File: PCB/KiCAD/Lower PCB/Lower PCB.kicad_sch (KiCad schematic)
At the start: 94 parts, among them IC1 ADG608BRZ, IC2 ADG608BRZ, J1 Conn_01x04, J2 Conn_01x02, J3 Conn_01x08, Q1 SFH320, Q10 SFH320, Q11 SFH320, Q12 SFH320, Q13 SFH320, Q14 SFH320, Q15 SFH320, Q16 SFH320, Q2 SFH320, Q3 SFH320, Q4 SFH320, Q5 SFH320, Q6 SFH320, Q7 SFH320, Q8 SFH320, Q9 SFH320, U1 ATmega328PB-A, Y1 Crystal

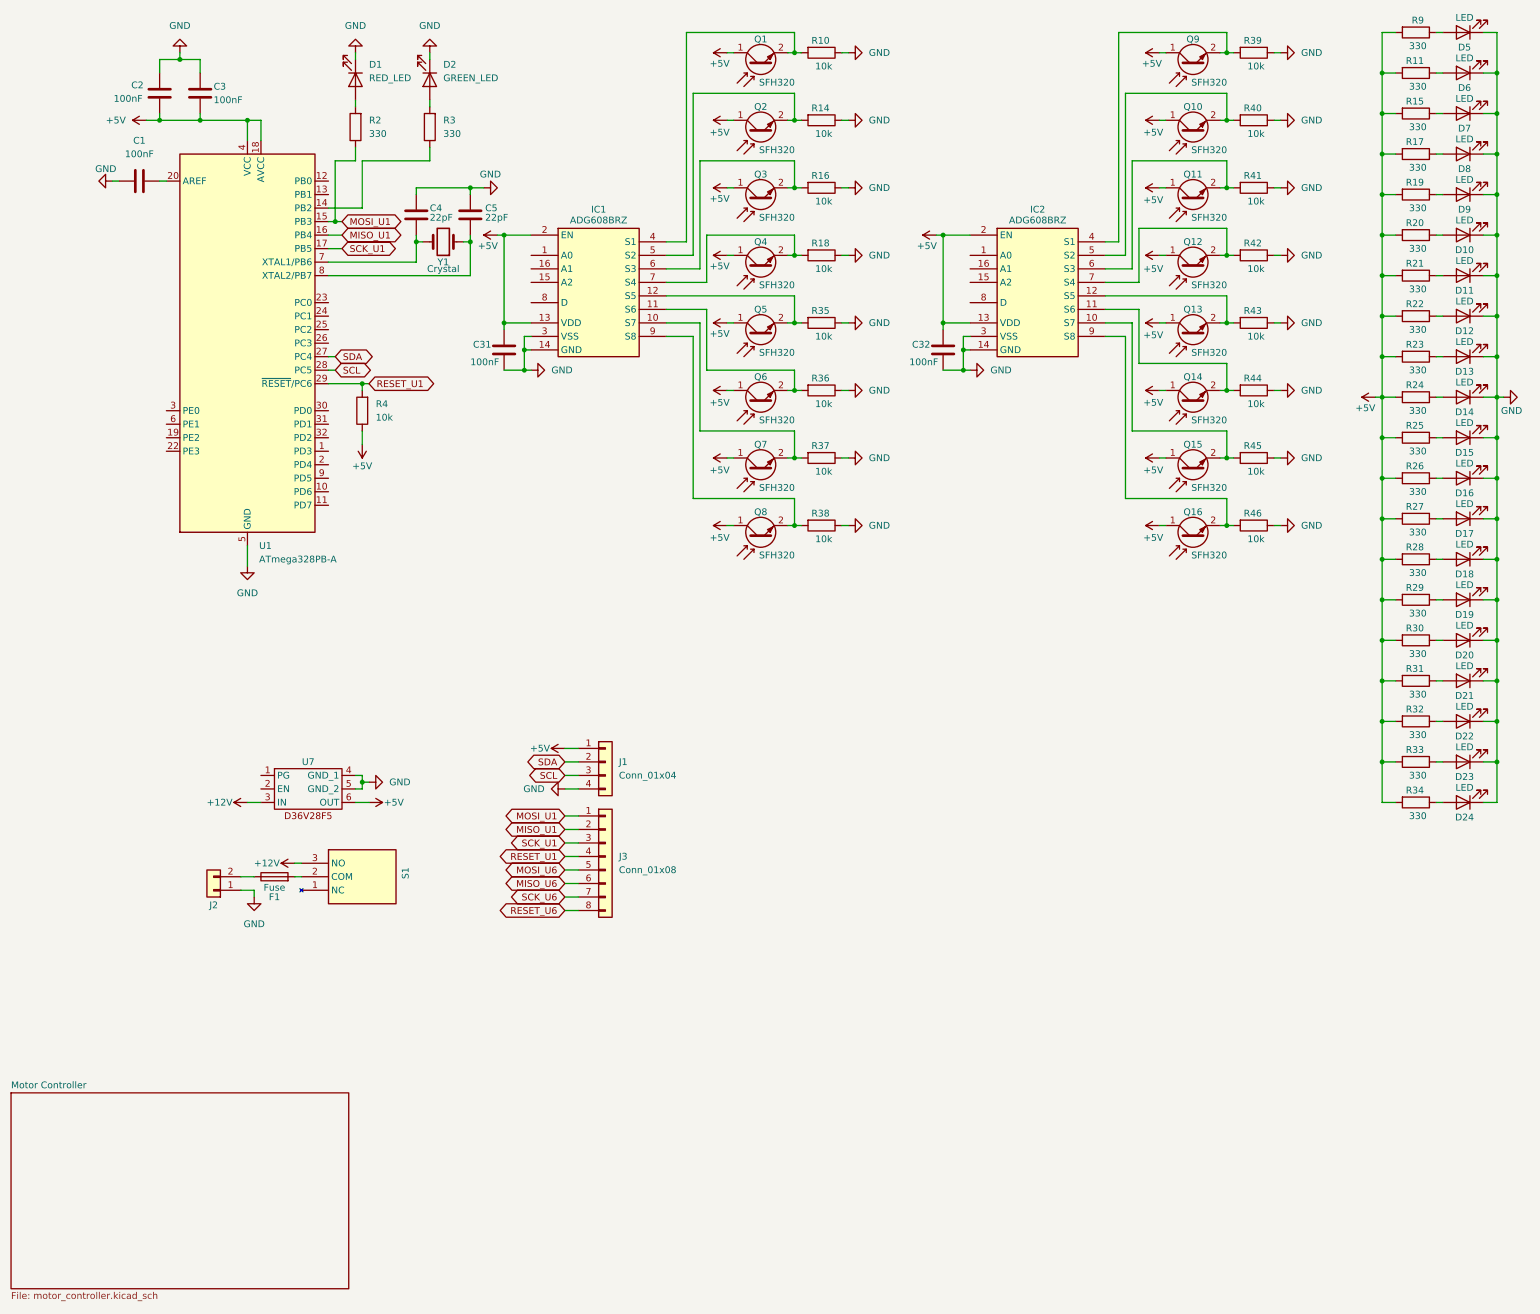
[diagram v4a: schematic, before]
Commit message: Redone main PCB traces and started lower PCB
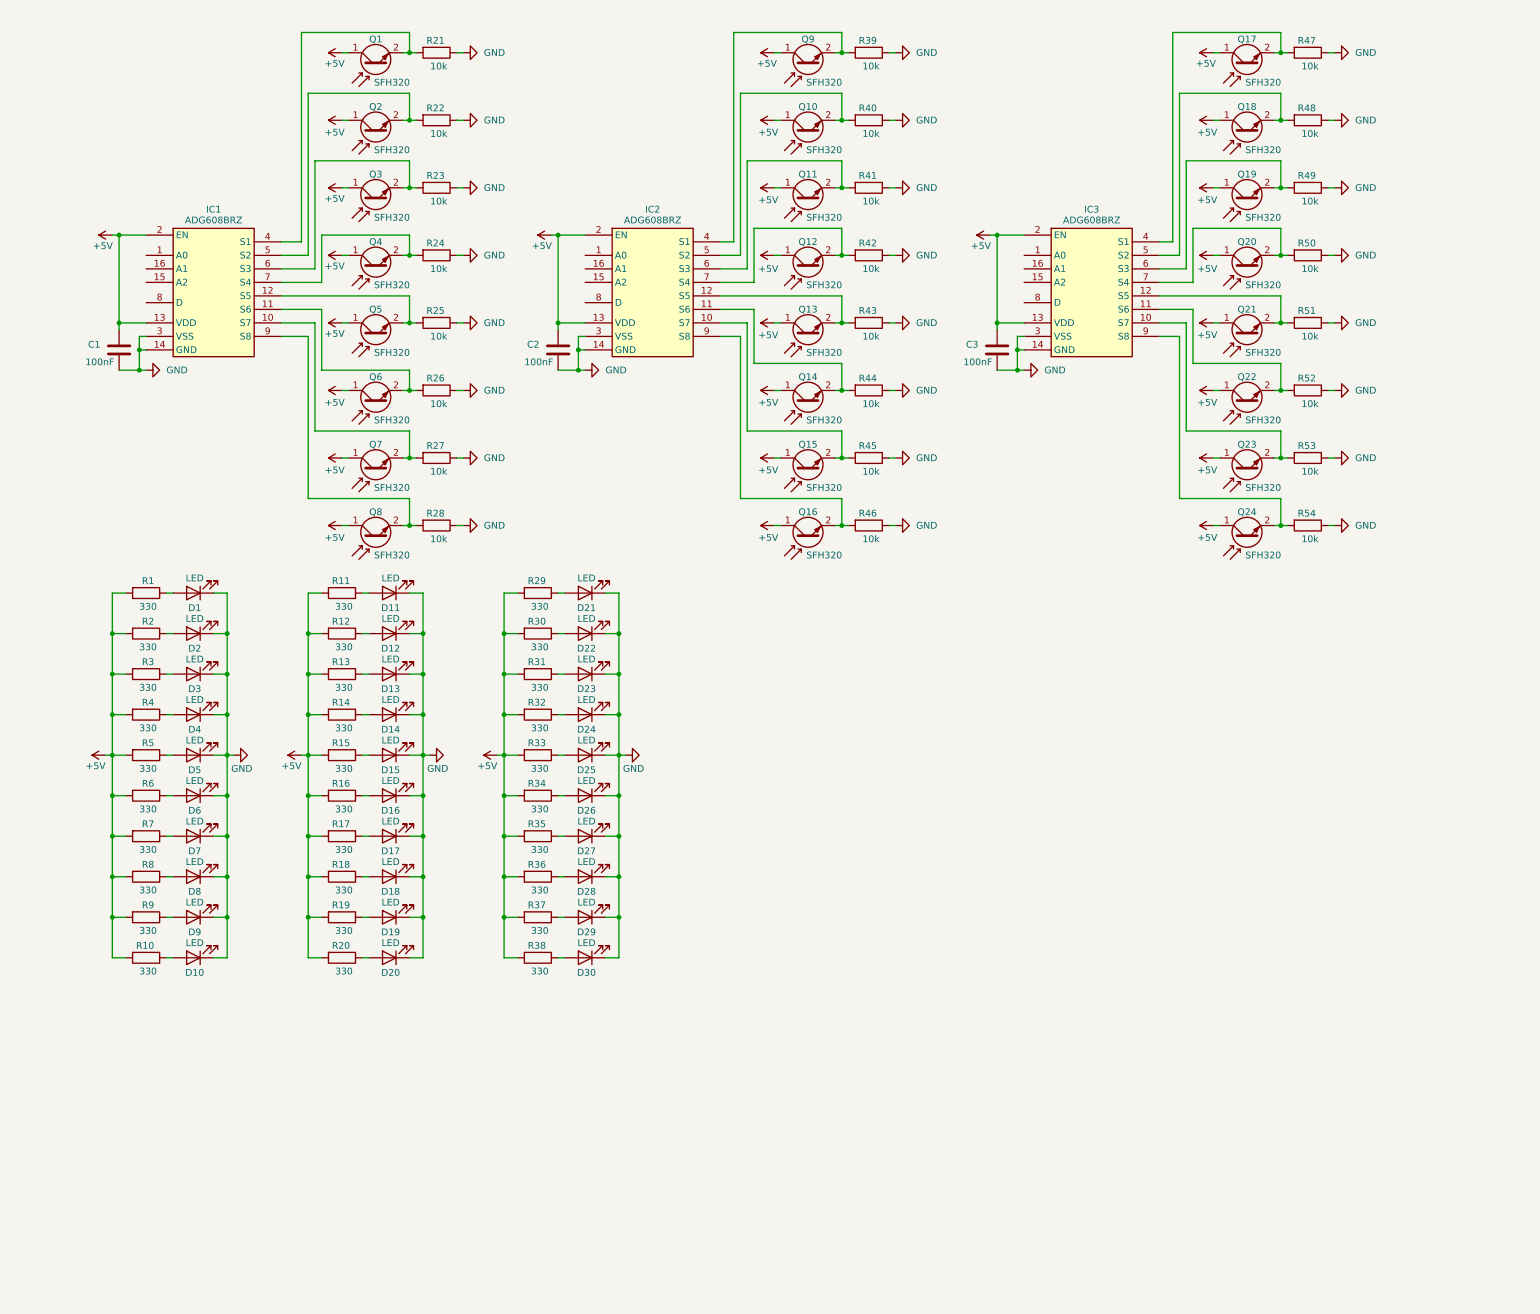
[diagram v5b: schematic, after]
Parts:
- removed C1, C2: 100nF, Capacitor_SMD:C_0805_2012Metric_Pad1.18x1.45mm_HandSolder, symbol Device:C
- removed C4, C5: 22pF, Capacitor_SMD:C_0805_2012Metric_Pad1.18x1.45mm_HandSolder, symbol Device:C
- removed D1: RED_LED, LED_SMD:LED_0805_2012Metric_Pad1.15x1.40mm_HandSolder, symbol Device:LED
- removed D2: GREEN_LED, LED_SMD:LED_0805_2012Metric_Pad1.15x1.40mm_HandSolder, symbol Device:LED
- removed F1: Fuse, Fuse:Fuseholder_Blade_Mini_Keystone_3568, symbol Device:Fuse
- removed J1: Conn_01x04, Connector_JST:JST_PH_B4B-PH-K_1x04_P2.00mm_Vertical, symbol Connector_Generic:Conn_01x04
- removed J2: Conn_01x02, Connector_AMASS:AMASS_XT60-M_1x02_P7.20mm_Vertical, symbol Connector_Generic:Conn_01x02
- removed J3: Conn_01x08, Connector_JST:JST_PH_B8B-PH-K_1x08_P2.00mm_Vertical, symbol Connector_Generic:Conn_01x08
- removed R2, R3: 330, Resistor_SMD:R_0805_2012Metric_Pad1.20x1.40mm_HandSolder, symbol Device:R
- removed R4: 10k, Resistor_SMD:R_0805_2012Metric_Pad1.20x1.40mm_HandSolder, symbol Device:R
- removed S1: 1101M2S3CGE2, 1101M2S3CGE2:1101M2S3CGE2, symbol 1101M2S3CGE2:1101M2S3CGE2
- removed U1: ATmega328PB-A, Package_QFP:TQFP-32_7x7mm_P0.8mm, symbol MCU_Microchip_ATmega:ATmega328PB-A
- removed U7: ~, Pololu:D36V28F5, symbol Pololu:D36V28F5
- removed Y1: Crystal, Crystal:Crystal_SMD_HC49-SD, symbol Device:Crystal
- added D21, D22, D23, D24, D25, D26, D27, D28, D29, D30: LED, LED_SMD:LED_PLCC-2_3.4x3.0mm_KA, symbol Device:LED
- added IC3: ADG608BRZ, ADG608BRZ:SOIC127P600X175-16N, symbol ADG608BRZ:ADG608BRZ
- added Q17, Q18, Q19, Q20, Q21, Q22, Q23, Q24: SFH320, LED_SMD:LED_PLCC-2_3.4x3.0mm_KA, symbol Sensor_Optical:SFH320
- added R29, R30, R31, R32, R33, R34, R35, R36, R37, R38: 330, Resistor_SMD:R_0805_2012Metric_Pad1.20x1.40mm_HandSolder, symbol Device:R
- added R47, R48, R49, R50, R51, R52, R53, R54: 10k, Resistor_SMD:R_0805_2012Metric_Pad1.20x1.40mm_HandSolder, symbol Device:R
- renumbered C31 to C1, C32 to C2, D5 to D1, D14 to D10, D15 to D11, D16 to D12, D17 to D13, D18 to D14, D19 to D15, D20 to D16, D21 to D17, D22 to D18, D23 to D19, D6 to D2, D24 to D20, D7 to D3, D8 to D4, D9 to D5, D10 to D6, D11 to D7, D12 to D8, D13 to D9, R9 to R1, R24 to R10, R25 to R11, R26 to R12, R27 to R13, R28 to R14, R29 to R15, R30 to R16, R31 to R17, R32 to R18, R33 to R19, R11 to R2, R34 to R20, R10 to R21, R14 to R22, R16 to R23, R18 to R24, R35 to R25, R36 to R26, R37 to R27, R38 to R28, R15 to R3, R17 to R4, R19 to R5, R20 to R6, R21 to R7, R22 to R8, R23 to R9
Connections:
- net +5V: now also C3.1, IC3.13 (VDD), IC3.2 (EN), Q17.1 (C), Q18.1 (C), Q19.1 (C), Q20.1 (C), Q21.1 (C), Q22.1 (C), Q23.1 (C), Q24.1 (C), R29.2, R30.2, R31.2, R32.2, R33.2, R34.2, R35.2, R36.2, R37.2, R38.2; no longer C3.2
- net GND: now also C3.2, D21.1 (K), D22.1 (K), D23.1 (K), D24.1 (K), D25.1 (K), D26.1 (K), D27.1 (K), D28.1 (K), D29.1 (K), D30.1 (K), IC3.14 (GND), IC3.3 (VSS), R47.1, R48.1, R49.1, R50.1, R51.1, R52.1, R53.1, R54.1; no longer C3.1
- new net: IC3.9 (S8), Q24.2 (E), R54.2
- new net: IC3.12 (S5), Q21.2 (E), R51.2
- new net: D30.2 (A), R38.1
- new net: IC3.7 (S4), Q20.2 (E), R50.2
- new net: D27.2 (A), R35.1
- new net: IC3.4 (S1), Q17.2 (E), R47.2
- new net: D23.2 (A), R31.1
- new net: D24.2 (A), R32.1
- new net: IC3.11 (S6), Q22.2 (E), R52.2
- new net: IC3.10 (S7), Q23.2 (E), R53.2
- new net: D26.2 (A), R34.1
- new net: D21.2 (A), R29.1
- new net: D28.2 (A), R36.1
- new net: IC3.6 (S3), Q19.2 (E), R49.2
- new net: IC3.5 (S2), Q18.2 (E), R48.2
- new net: D29.2 (A), R37.1
- new net: D25.2 (A), R33.1
- new net: D22.2 (A), R30.1
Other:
- removed sheet Motor Controller
- moved on the sheet: C1, C2, D1, D10, D11, D12, D13, D14, D15, D16, D17, D18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

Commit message: Work on the lower PCB
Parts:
- added J1, J2, J3: Conn_01x04_MountingPin, Connector_JST:JST_PH_B4B-PH-SM4-TB_1x04-1MP_P2.00mm_Vertical, symbol Connector_Generic_MountingPin:Conn_01x04_MountingPin
- added J4: Conn_01x02_MountingPin, Connector_JST:JST_PH_B2B-PH-SM4-TB_1x02-1MP_P2.00mm_Vertical, symbol Connector_Generic_MountingPin:Conn_01x02_MountingPin
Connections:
- net GND: now also J4.2 (Pin_2)
- new net +3V3: J4.1 (Pin_1)
- new net LED_1_A0: J1.2 (Pin_2)
- new net LED_1_A1: J1.3 (Pin_3)
- new net LED_1_A2: J1.4 (Pin_4)
- new net LED_1_OUT: J1.1 (Pin_1)
- new net LED_2_A0: J2.2 (Pin_2)
- new net LED_2_A1: J2.3 (Pin_3)
- new net LED_2_A2: J2.4 (Pin_4)
- new net LED_2_OUT: J2.1 (Pin_1)
- new net LED_3_A0: J3.2 (Pin_2)
- new net LED_3_A1: J3.3 (Pin_3)
- new net LED_3_A2: J3.4 (Pin_4)
- new net LED_3_OUT: J3.1 (Pin_1)

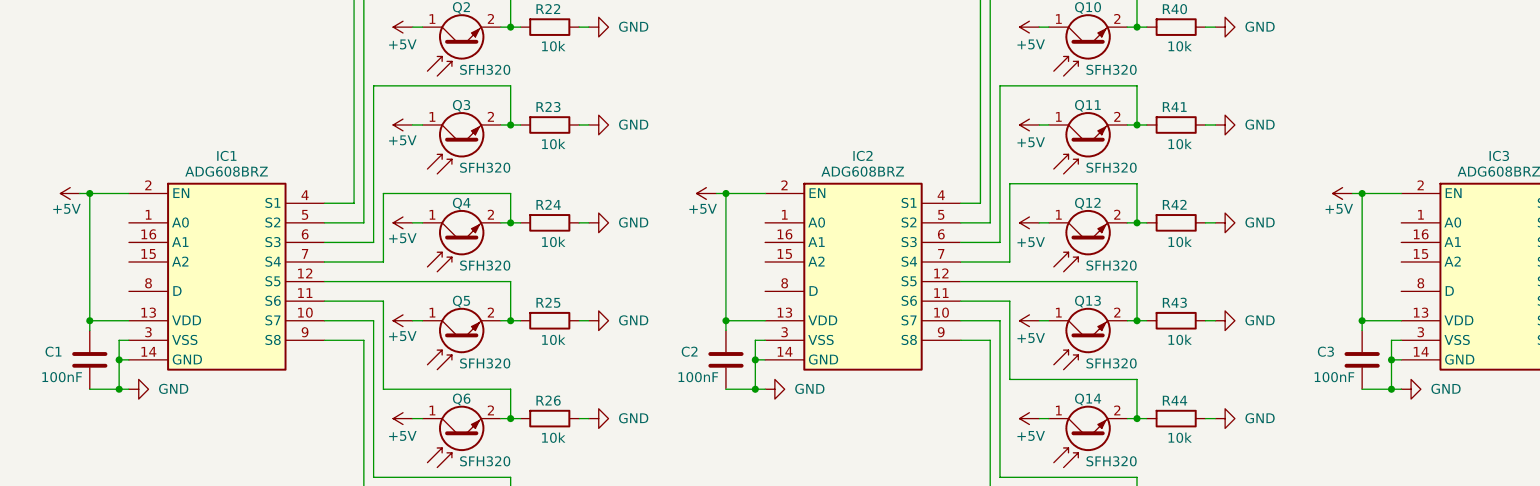
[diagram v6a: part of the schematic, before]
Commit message: Started aranging the LDRs and LEDs
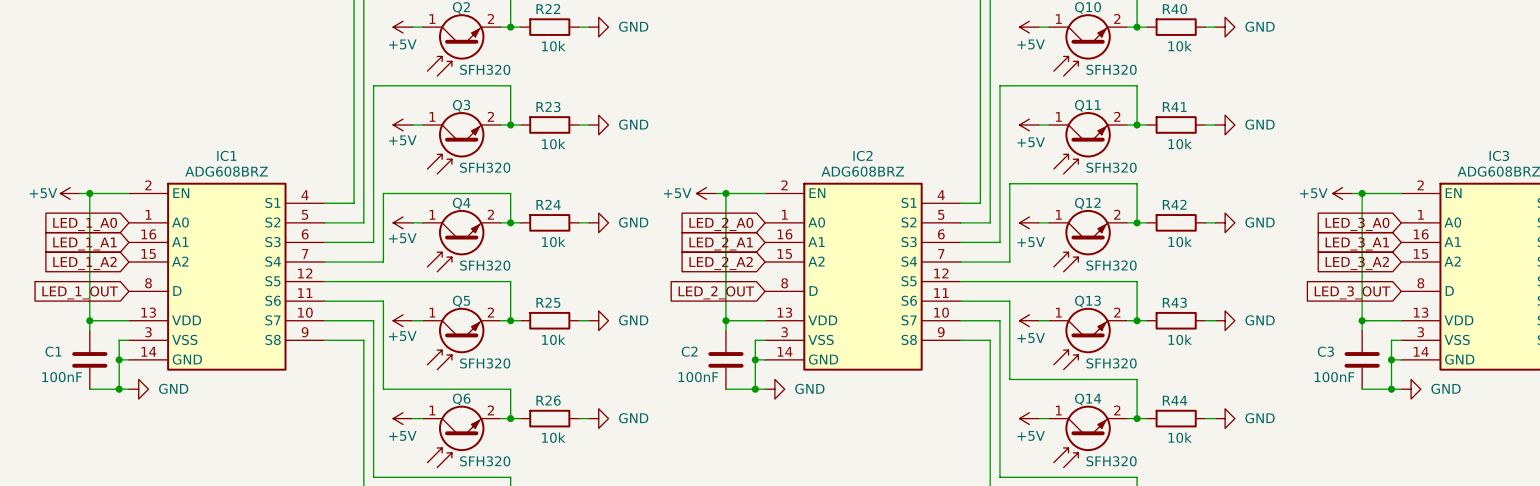
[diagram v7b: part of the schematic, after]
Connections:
- net LED_1_A0: now also IC1.1 (A0)
- net LED_1_A1: now also IC1.16 (A1)
- net LED_1_A2: now also IC1.15 (A2)
- net LED_1_OUT: now also IC1.8 (D)
- net LED_2_A0: now also IC2.1 (A0)
- net LED_2_A1: now also IC2.16 (A1)
- net LED_2_A2: now also IC2.15 (A2)
- net LED_2_OUT: now also IC2.8 (D)
- net LED_3_A0: now also IC3.1 (A0)
- net LED_3_A1: now also IC3.16 (A1)
- net LED_3_A2: now also IC3.15 (A2)
- net LED_3_OUT: now also IC3.8 (D)
